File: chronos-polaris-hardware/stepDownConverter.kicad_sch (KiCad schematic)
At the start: 7 parts, among them U11 TPS62172DSGR

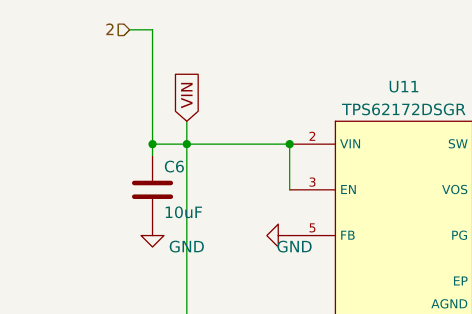
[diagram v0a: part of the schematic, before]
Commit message: changed label names. - Rishik B.
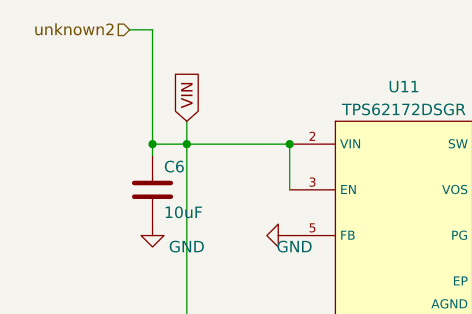
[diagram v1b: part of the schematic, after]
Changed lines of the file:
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@@
 		)
 	)
-	(hierarchical_label "2"
+	(hierarchical_label "unknown2"
 		(shape input)
 		(at 96.52 64.77 180)

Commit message: asdf
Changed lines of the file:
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@@
 		)
 	)
-	(hierarchical_label "unknown2"
+	(hierarchical_label "VIN"
 		(shape input)
 		(at 96.52 64.77 180)

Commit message: made satvik fixes
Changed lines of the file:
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@@
+	)
+	(junction
+		(at 158.75 77.47)
+		(diameter 0)
+		(color 0 0 0 0)
 	)
 	(junction
@@
 	(wire
 		(pts
-			(xy 102.87 74.93) (xy 102.87 77.47)
-		)
-		(stroke
-			(width 0)
-			(type default)
-		)
-	)
-	(wire
-		(pts
 			(xy 102.87 77.47) (xy 102.87 109.22)
 		)
@@
 	(wire
 		(pts
-			(xy 96.52 116.84) (xy 102.87 116.84)
-		)
-		(stroke
-			(width 0)
-			(type default)
-		)
-	)
-	(wire
-		(pts
 			(xy 99.06 77.47) (xy 102.87 77.47)
 		)
@@
 	(wire
 		(pts
+			(xy 92.71 116.84) (xy 102.87 116.84)
+		)
+		(stroke
+			(width 0)
+			(type default)
+		)
+	)
+	(wire
+		(pts
 			(xy 114.3 77.47) (xy 114.3 82.55)
 		)
@@
 	(wire
 		(pts
+			(xy 158.75 77.47) (xy 167.64 77.47)
+		)
+		(stroke
+			(width 0)
+			(type default)
+		)
+	)
+	(wire
+		(pts
 			(xy 142.24 92.71) (xy 140.97 92.71)
 		)
@@
 		)
 	)
-	(global_label "3.3V"
+	(hierarchical_label "VIN"
 		(shape input)
-		(at 158.75 77.47 90)
+		(at 96.52 64.77 180)
+		(fields_autoplaced yes)
+		(effects
+			(font
+				(size 1.27 1.27)
+			)
+			(justify right)
+		)
+	)
+	(hierarchical_label "3.3V"
+		(shape input)
+		(at 167.64 77.47 0)
 		(fields_autoplaced yes)
 		(effects
@@
 			(justify left)
 		)
-		(property "Intersheetrefs" "${INTERSHEET_REFS}"
-			(at 158.75 70.4518 90)
-			(effects
-				(font
-					(size 1.27 1.27)
-				)
-				(justify left)
-				(hide yes)
-			)
-		)
-	)
-	(global_label "VIN_1{slash}4"
+	)
+	(hierarchical_label "VIN_1{slash}4"
 		(shape input)
-		(at 96.52 116.84 180)
+		(at 92.71 116.84 180)
 		(fields_autoplaced yes)
 		(effects
-			(font
-				(size 1.27 1.27)
-			)
-			(justify right)
-		)
-		(property "Intersheetrefs" "${INTERSHEET_REFS}"
-			(at 85.8732 116.84 0)
-			(effects
-				(font
-					(size 1.27 1.27)
-				)
-				(justify right)
-				(hide yes)
-			)
-		)
-	)
-	(global_label "VIN"
-		(shape input)
-		(at 102.87 74.93 90)
-		(fields_autoplaced yes)
-		(effects
-			(font
-				(size 1.27 1.27)
-			)
-			(justify left)
-		)
-		(property "Intersheetrefs" "${INTERSHEET_REFS}"
-			(at 102.87 69.0003 90)
-			(effects
-				(font
-					(size 1.27 1.27)
-				)
-				(justify left)
-				(hide yes)
-			)
-		)
-	)
-	(hierarchical_label "VIN"
-		(shape input)
-		(at 96.52 64.77 180)
-		(fields_autoplaced yes)
-		(effects

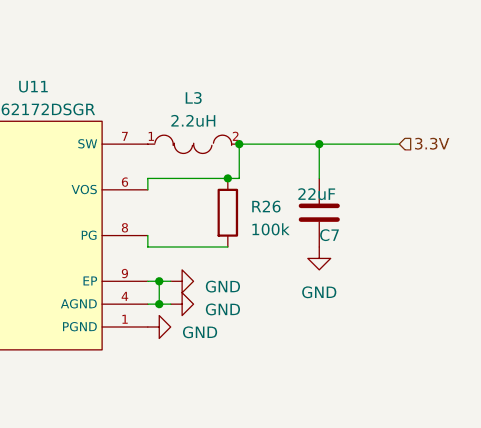
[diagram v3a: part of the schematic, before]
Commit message: E-match lowside switch
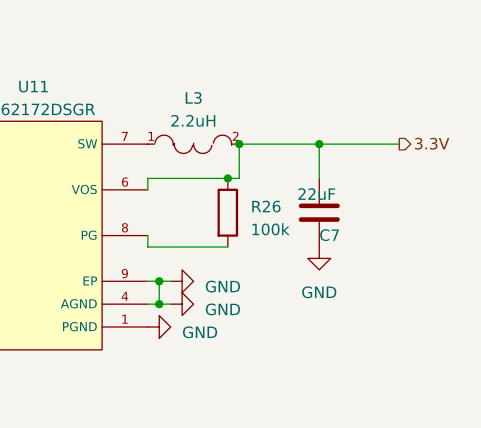
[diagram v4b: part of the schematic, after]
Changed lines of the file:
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@@
 	)
 	(hierarchical_label "3.3V"
-		(shape input)
+		(shape output)
 		(at 167.64 77.47 0)
 		(fields_autoplaced yes)

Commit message: Fixed warnings and error messages. - Rishik B.
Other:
- moved on the sheet: L3

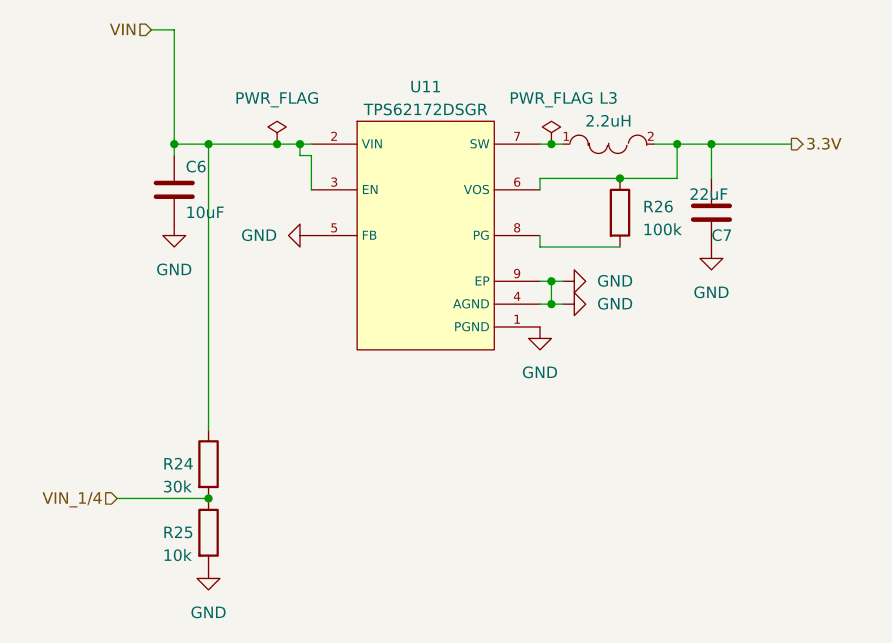
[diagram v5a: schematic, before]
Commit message: Schematic Changes as per DR1 Suggestions
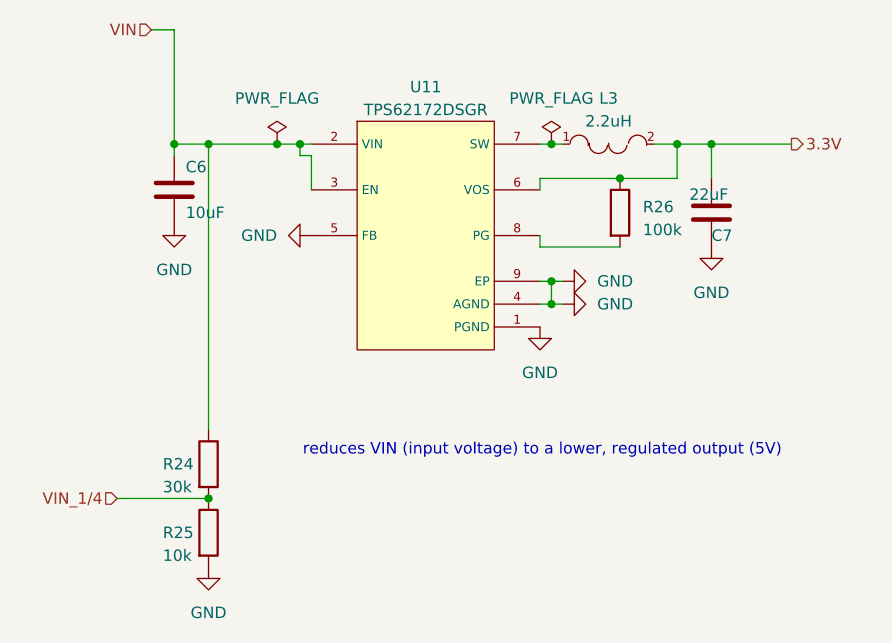
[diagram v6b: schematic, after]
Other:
- note added: "reduces VIN (input voltage) to a lower, regulated output (5V)"
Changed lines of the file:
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@@
+		)
+	)
+	(text "reduces VIN (input voltage) to a lower, regulated output (5V)"
+		(exclude_from_sim no)
+		(at 139.954 111.506 0)
+		(effects
+			(font
+				(size 1.27 1.27)
+			)
 		)
 	)
